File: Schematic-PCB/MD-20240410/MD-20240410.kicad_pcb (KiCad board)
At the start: 2 copper layers, 100.5 x 56.4 mm, 50 parts, among them J2 Conn_01x04_Pin, J3 Conn_01x02_Pin, J4 Conn_01x02_Pin, J5 Conn_01x02_Pin, J6 Conn_01x02_Pin, J7 Conn_01x02_Pin, Q2 PMOS, Q3 NMOS, Q4 NMOS

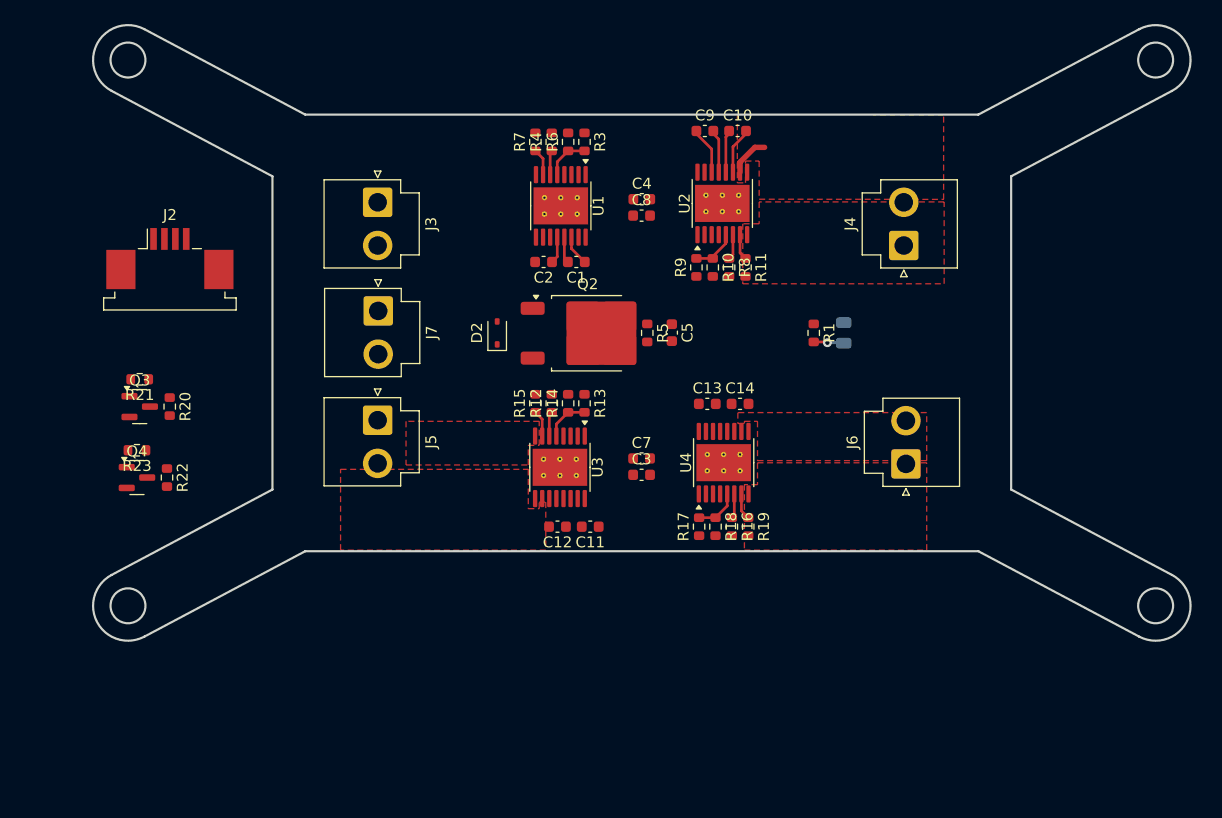
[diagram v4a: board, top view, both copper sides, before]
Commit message: MD基板・メイン基板の回路図を更新
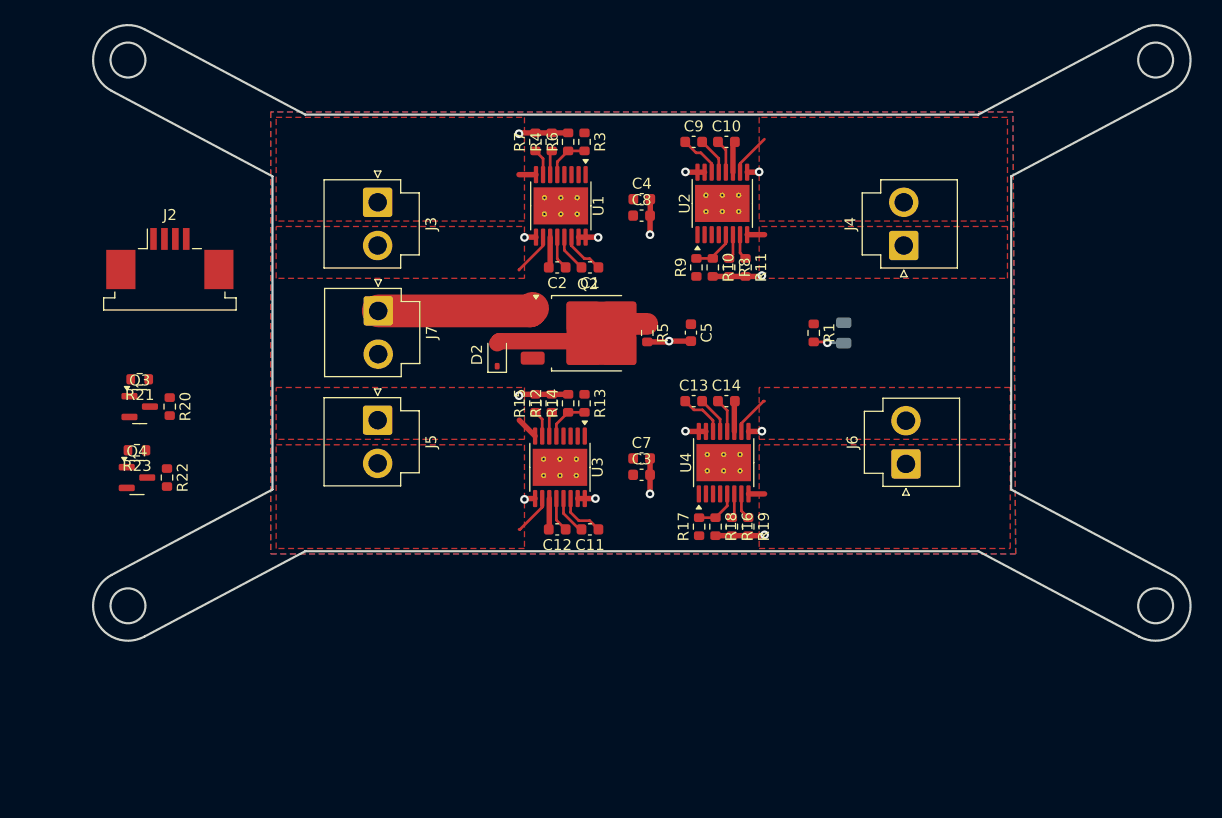
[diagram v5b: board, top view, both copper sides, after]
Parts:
- moved D2 2.00 mm to (136.8, 89.5)
- moved C5 1.75 mm to (154.5, 87.5)
- moved C10 1.43 mm to (157.8, 70.0)
- moved C9 1.43 mm to (154.8, 70.0)
- moved C1 1.35 mm to (145.2, 81.5)
- moved C2 1.35 mm to (142.2, 81.5)
- moved C13 1.27 mm to (154.8, 93.8)
- moved C14 1.27 mm to (157.8, 93.8)
- moved C11 0.25 mm to (145.2, 105.5)
- moved C12 0.25 mm to (142.2, 105.5)
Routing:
- net GND: track 0.00 -> 40.2 mm, vias 0 -> 15
- net VCC: track 0.00 -> 14.2 mm
- net Net-(D2-A): track 0.00 -> 12.7 mm
- net VM: track 4.02 -> 11.3 mm
- net Net-(U3-CPL): track 0.00 -> 4.47 mm
- net Net-(U4-CPL): track 0.00 -> 4.29 mm
- net OUT2-1: track 0.00 -> 3.94 mm
- net OUT2-3: track 0.00 -> 3.76 mm
- net OUT2-4: track 0.00 -> 3.71 mm
- net Net-(U3-CPH): track 0.00 -> 3.62 mm
- net Net-(U4-CPH): track 0.00 -> 3.46 mm
- net Net-(U3-VCP): track 0.00 -> 3.18 mm
- net Net-(U4-VCP): track 0.00 -> 3.13 mm
- net OUT1-3: track 0.00 -> 2.05 mm
- net OUT1-2: track 0.00 -> 1.60 mm
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- added copper zone on B.Cu, net GND
- added copper zone on F.Cu, net OUT1-1
- added copper zone on F.Cu, net OUT2-1
- added copper zone on F.Cu, net VM

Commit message: MD・ラインセンサの回路を更新しました
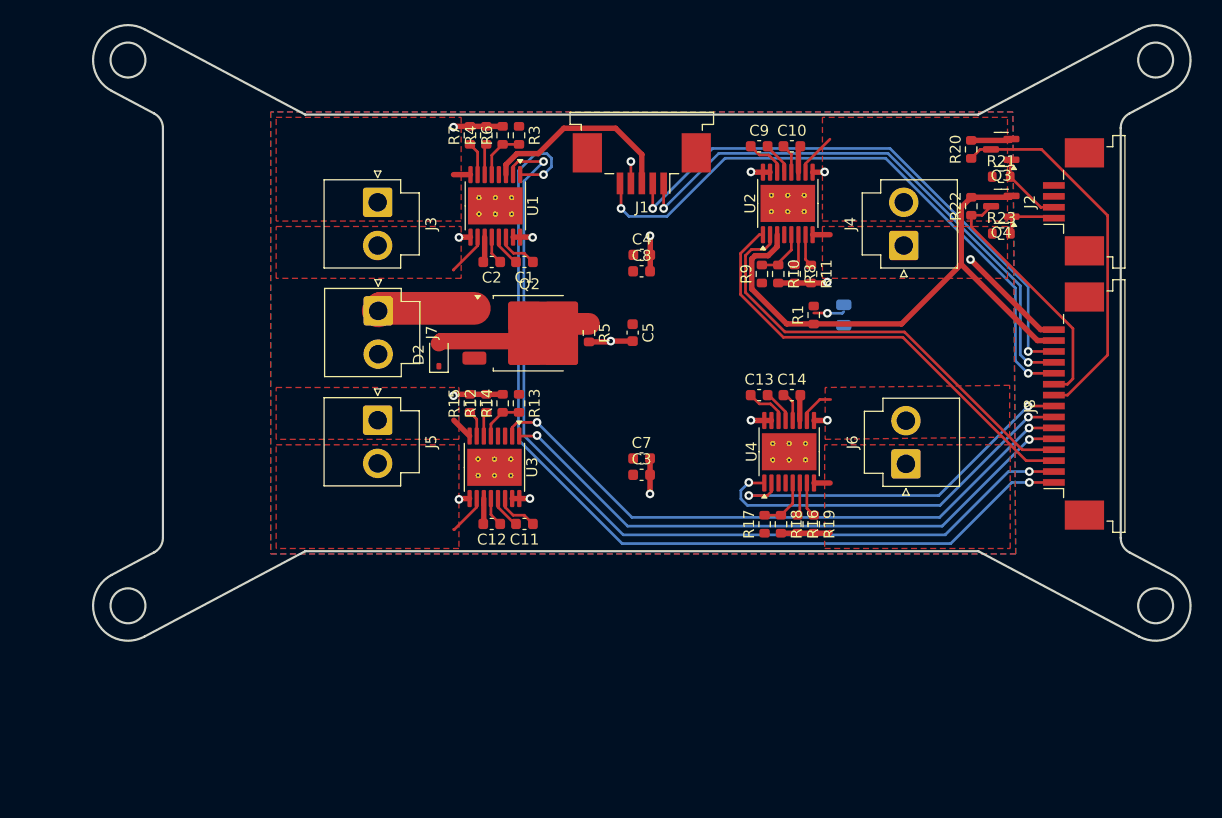
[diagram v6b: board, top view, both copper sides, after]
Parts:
- added J1: Conn_01x05_Pin, Connector_FFC-FPC:TE_84953-5_1x05-1MP_P1.0mm_Horizontal, F.Cu at (150.0, 72.0)
- added J8: Conn_01x15_Pin, Connector_FFC-FPC:TE_1-84953-5_1x15-1MP_P1.0mm_Horizontal, F.Cu at (189.6, 94.2)
- moved Q4 83.0 mm to (182.9, 75.9), turned to 180 degrees
- moved J2 82.9 mm to (189.6, 75.5), turned to 90 degrees
- moved Q3 82.4 mm to (182.9, 70.7), turned to 180 degrees
- moved R23 81.6 mm to (182.9, 78.4), turned to 0 degrees
- moved R21 81.1 mm to (182.9, 73.2), turned to 0 degrees
- moved R22 77.8 mm to (180.2, 75.9), turned to 90 degrees
- moved R20 77.1 mm to (180.2, 70.7), turned to 90 degrees
- moved U4 6.08 mm to (163.5, 98.4)
- moved R10 6.03 mm to (162.5, 82.1)
- moved R11 6.03 mm to (165.5, 82.1)
- moved R3 6.03 mm to (138.8, 69.4)
- moved R4 6.03 mm to (135.8, 69.4)
- moved R6 6.03 mm to (137.2, 69.4)
- moved R7 6.03 mm to (134.2, 69.4)
- moved R8 6.03 mm to (164.0, 82.1)
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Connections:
- J2 pad 1: Line-MD-Main=RX_5V -> Line-MD-Main=TX_5V
- J2 pad 2: Line-MD-Main=TX_5V -> Line-MD-Main=RX_5V
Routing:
- net EN-1: track 0.00 -> 87.8 mm, vias 0 -> 2
- net PH-1: track 0.00 -> 84.3 mm, vias 0 -> 2
- net +3.3V: track 0.00 -> 73.2 mm
- net PH-3: track 0.00 -> 57.6 mm, vias 0 -> 2
- net ball01k: track 0.00 -> 56.5 mm, vias 0 -> 2
- net EN-3: track 0.00 -> 55.8 mm, vias 0 -> 2
- net KickerSignal-main: track 0.00 -> 52.5 mm, vias 0 -> 2
- net ball02k: track 0.00 -> 51.8 mm, vias 0 -> 2
- net EN-2: track 0.00 -> 41.5 mm
- net PH-2: track 0.00 -> 41.1 mm
- net EN-4: track 0.00 -> 35.5 mm, vias 0 -> 2
- net Line-MD-Main=RX_3.3V: track 0.00 -> 34.6 mm
- net PH-4: track 0.00 -> 34.4 mm, vias 0 -> 2
- net Line-MD-Main=TX_3.3V: track 0.00 -> 22.9 mm
- net GND: track 40.2 -> 52.3 mm, vias 15 -> 16
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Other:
- outline, holes or cut-outs redrawn

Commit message: MDのPCBを更新
・XT30コネクタへの変更
・DRV8874のビア・オン・パッドの修正
・ベタの拡張
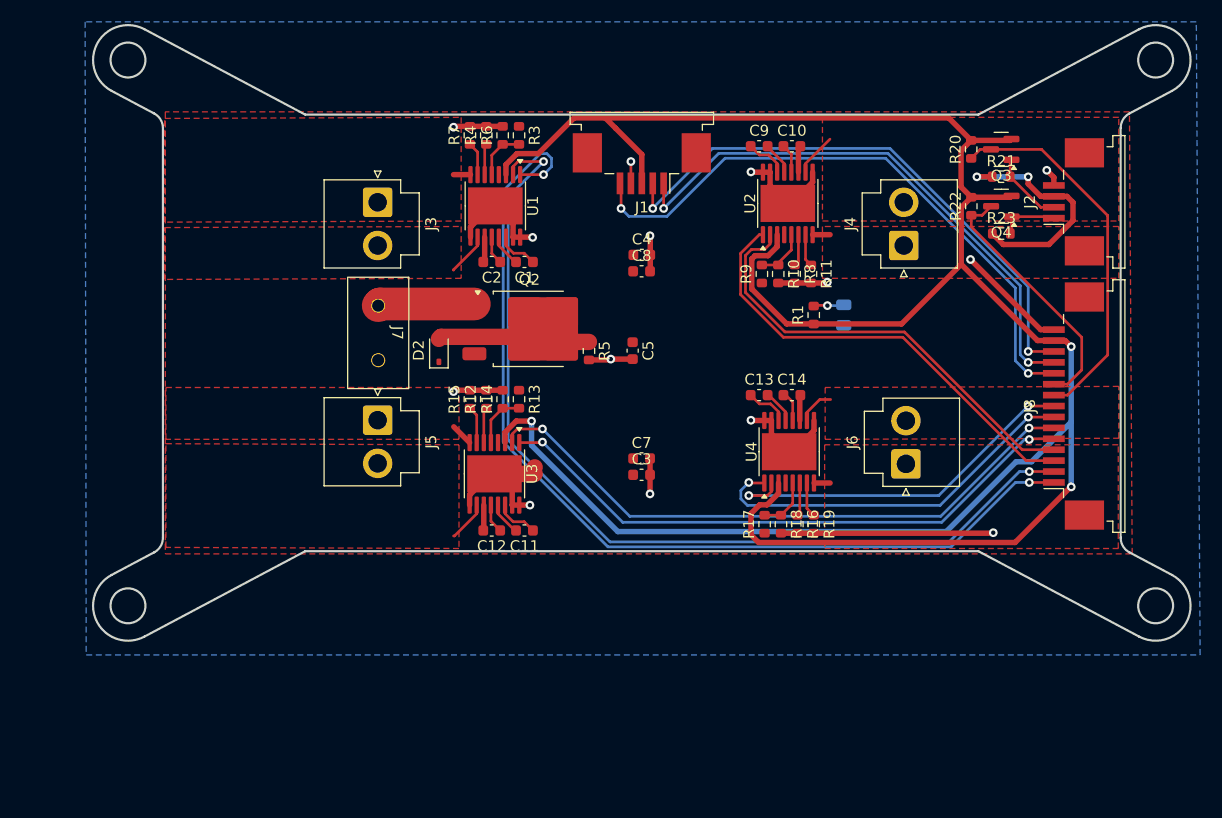
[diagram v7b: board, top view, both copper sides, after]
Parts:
- J7: footprint Connector_JST:JST_VH_B2P-VH_1x02_P3.96mm_Vertical -> @MyLibrary:XT30U-M
- U1, U2, U3, U4: footprint Package_SO:HTSSOP-16-1EP_4.4x5mm_P0.65mm_EP3.4x5mm_Mask2.46x2.31mm_ThermalVias -> Package_SO:HTSSOP-16-1EP_4.4x5mm_P0.65mm_EP3.4x5mm_Mask2.46x2.31mm
- moved J7 2.02 mm to (125.8, 87.5)
- moved C5 1.65 mm to (149.2, 89.1)
- moved R5 1.65 mm to (145.2, 89.2)
- moved C11 0.60 mm to (139.2, 105.6)
- moved C12 0.60 mm to (136.2, 105.6)
- moved U3 0.60 mm to (136.5, 100.4)
- moved D2 0.40 mm to (131.4, 89.1)
- moved Q2 0.40 mm to (139.7, 87.1)
- moved R12 0.38 mm to (135.8, 93.6)
- moved R13 0.38 mm to (138.8, 93.6)
- moved R14 0.38 mm to (137.2, 93.6)
- moved R15 0.38 mm to (134.2, 93.6)
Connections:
- U1 pad 17: (no net) -> GND
- U2 pad 17: (no net) -> GND
- U3 pad 17: (no net) -> GND
- U4 pad 17: (no net) -> GND
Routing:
- net +3.3V: track 73.2 -> 229.8 mm, vias 0 -> 3
- net GND: track 52.3 -> 98.3 mm, vias 16 -> 14
- net +5V: track 0.00 -> 21.9 mm, vias 0 -> 2
- net PH-1: track 84.3 -> 87.1 mm
- net EN-1: track 87.8 -> 89.9 mm
- net Net-(D2-A): track 12.7 -> 14.6 mm
- net VREF-3: track 4.12 -> 5.10 mm
- net Net-(U3-IPROPI): track 2.27 -> 3.24 mm
- net IMODE-3: track 2.43 -> 3.41 mm
- net Line-MD-Main=TX_3.3V: track 22.9 -> 23.6 mm
- net EN-3: track 55.8 -> 55.3 mm

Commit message: MD基板の仮完成
DRをお願いします
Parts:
- moved R20 16.6 mm to (173.2, 85.8)
- moved Q3 16.2 mm to (175.8, 85.2), turned to -90 degrees
- moved R21 13.4 mm to (178.2, 85.8), turned to 90 degrees
- moved R22 9.86 mm to (179.8, 85.8)
- moved Q4 9.38 mm to (182.2, 85.2), turned to -90 degrees
- moved R23 7.57 mm to (184.8, 85.8), turned to 90 degrees
- moved D1 0.66 mm to (168.2, 85.2)
- moved R1 0.66 mm to (165.5, 85.2)
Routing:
- net +3.3V: track 229.8 -> 209.8 mm, vias 3 -> 9
- net Line-MD-Main=RX_3.3V: track 34.6 -> 17.6 mm
- net Line-MD-Main=RX_5V: track 6.76 -> 19.5 mm
- net GND: track 98.3 -> 87.5 mm
- net EN-2: track 41.5 -> 50.5 mm, vias 0 -> 2
- net PH-1: track 87.1 -> 79.3 mm
- net PH-2: track 41.1 -> 48.9 mm, vias 0 -> 2
- net EN-1: track 89.9 -> 82.3 mm
- net Line-MD-Main=TX_5V: track 5.37 -> 11.0 mm
- net PH-4: track 34.4 -> 38.9 mm
- net EN-4: track 35.5 -> 40.0 mm
- net Line-MD-Main=TX_3.3V: track 23.6 -> 19.2 mm
- net PH-3: track 57.3 -> 61.3 mm
- net EN-3: track 55.3 -> 59.2 mm
- net ball01k: track 56.5 -> 58.4 mm
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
